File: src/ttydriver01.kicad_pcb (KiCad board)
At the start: 2 copper layers, 119.4 x 74.9 mm, 34 parts, among them P1 CONN_01X04, P2 CONN_01X02, P3 CONN_01X02, P4 CONN_01X10, Q1 IRLB8721PBF, T1 Coilcraft-DA2032, U1 NE555, U2 TPS2030P, U3 CP2102-breakout, U4 G3VM401E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

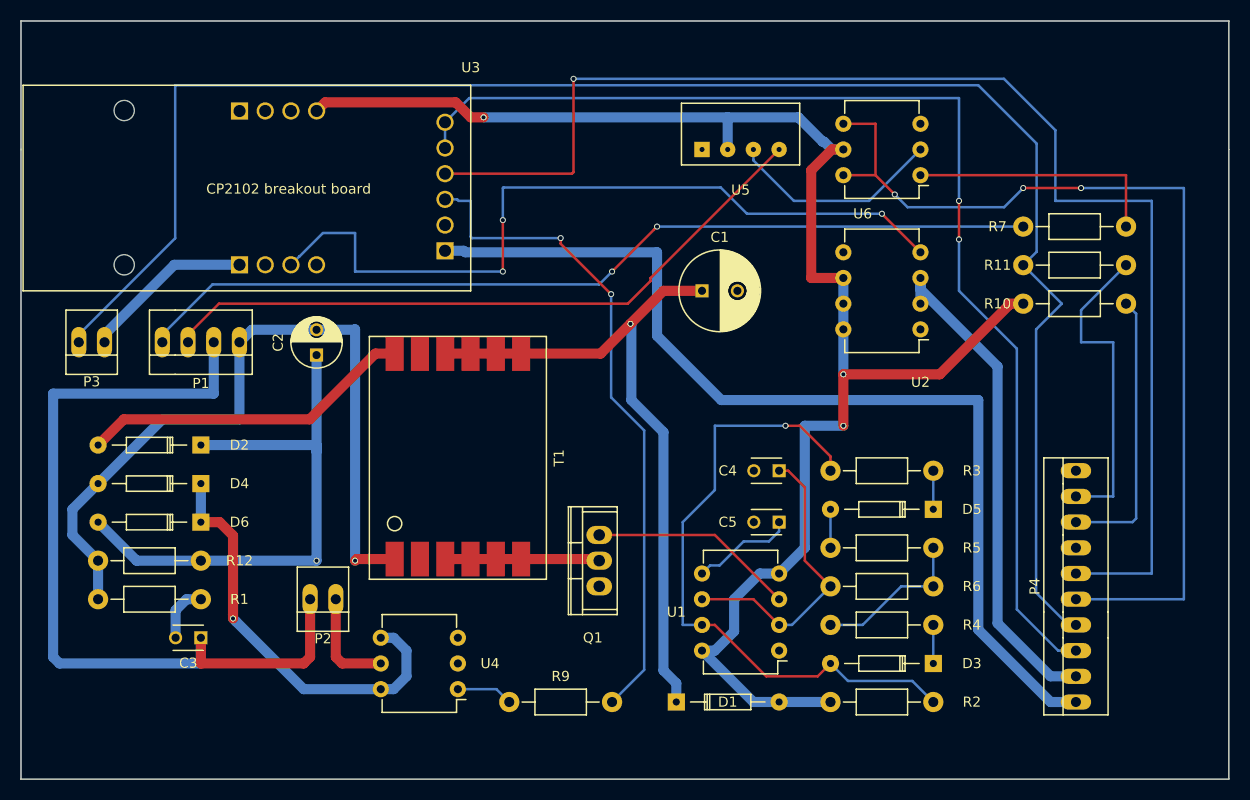
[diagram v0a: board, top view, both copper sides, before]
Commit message: Passes DRC. Valid board.  Still needs more cleanup.
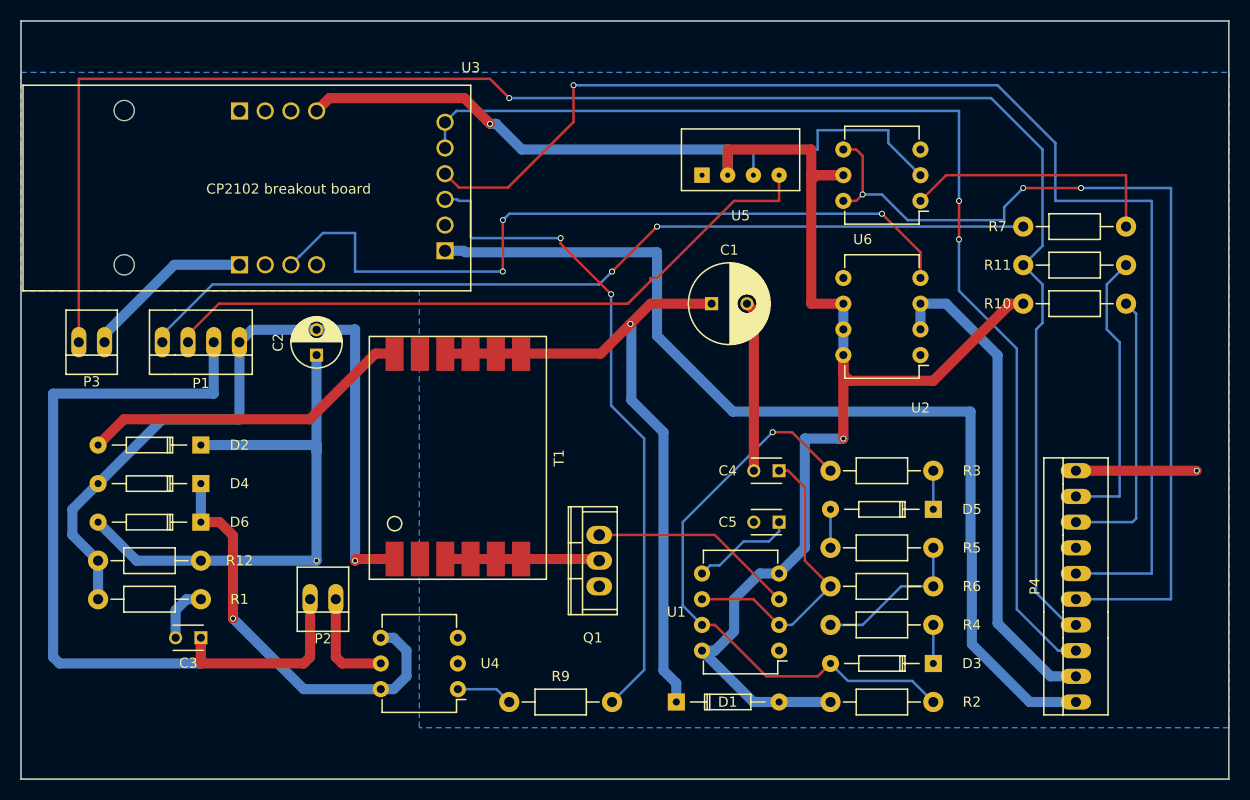
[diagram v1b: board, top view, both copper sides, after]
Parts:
- moved U6 2.54 mm to (144.8, 95.2)
- moved U2 2.54 mm to (144.8, 110.5)
- moved U5 2.54 mm to (127.0, 92.7)
- moved C1 1.58 mm to (124.1, 105.4)
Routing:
- net GND: track 17.0 -> 45.7 mm, vias 0 -> 1
- net Net-(D3-Pad2): track 64.1 -> 57.9 mm
- net Net-(P3-Pad2): track 169.7 -> 175.8 mm, vias 0 -> 1
- net VCC: track 157.6 -> 163.2 mm, vias 3 -> 2
- net /RxD: track 95.3 -> 91.8 mm
- net Net-(P4-Pad6): track 132.6 -> 129.1 mm
- net Net-(P4-Pad9): track 31.6 -> 28.5 mm
- net Net-(U5-Pad3): track 21.3 -> 23.5 mm
- net Net-(P4-Pad3): track 114.8 -> 113.0 mm
- net /ENABLE: track 78.3 -> 76.8 mm
- net Net-(R7-Pad2): track 25.4 -> 26.5 mm
- net Net-(P4-Pad2): track 49.7 -> 48.7 mm
- added copper zone on B.Cu, net GND

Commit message: Passes DRC. Valid board.  Still needs more cleanup.
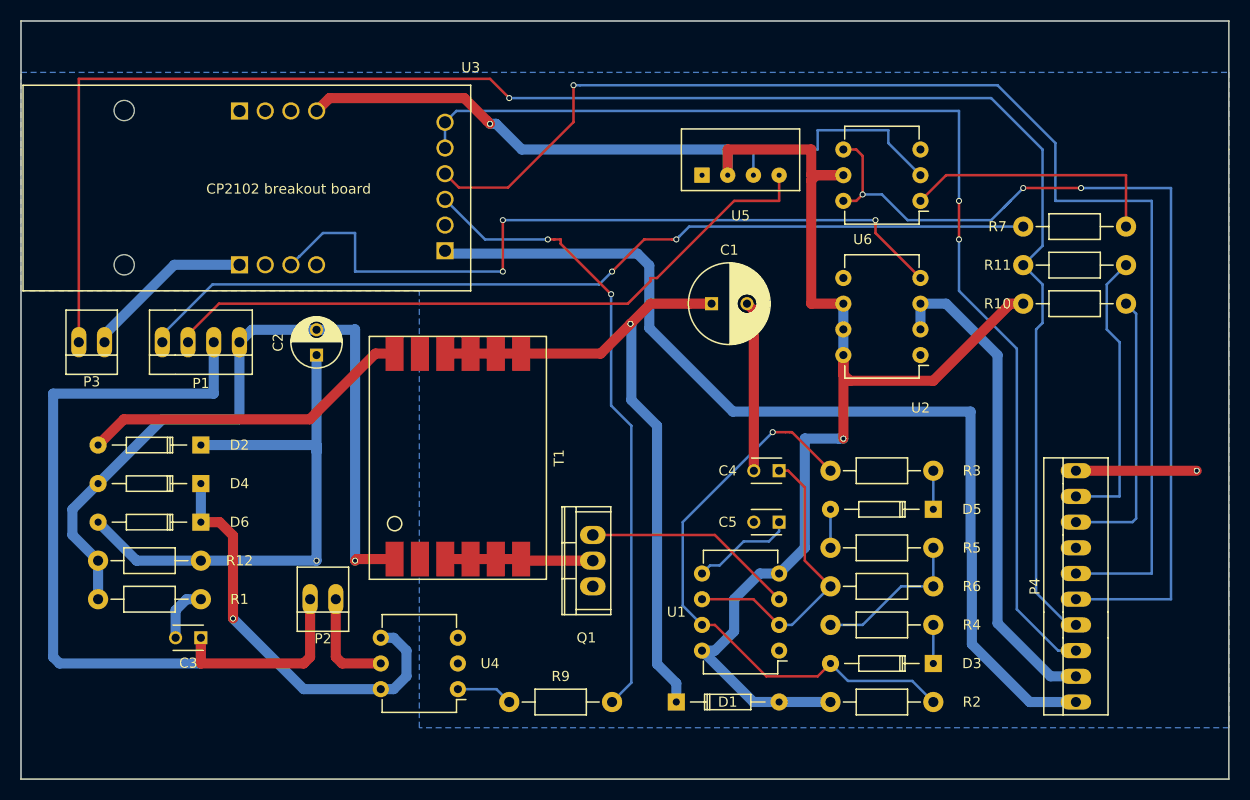
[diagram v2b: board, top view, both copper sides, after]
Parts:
- moved Q1 0.64 mm to (112.4, 130.8)
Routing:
- net /TxD: track 65.7 -> 62.7 mm
- net /ENABLE: track 76.8 -> 75.5 mm
- net Net-(P4-Pad1): track 99.1 -> 97.8 mm
- net /OSC: track 20.4 -> 21.0 mm

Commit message: Cleaned up copper fill. Almost ready for fab.
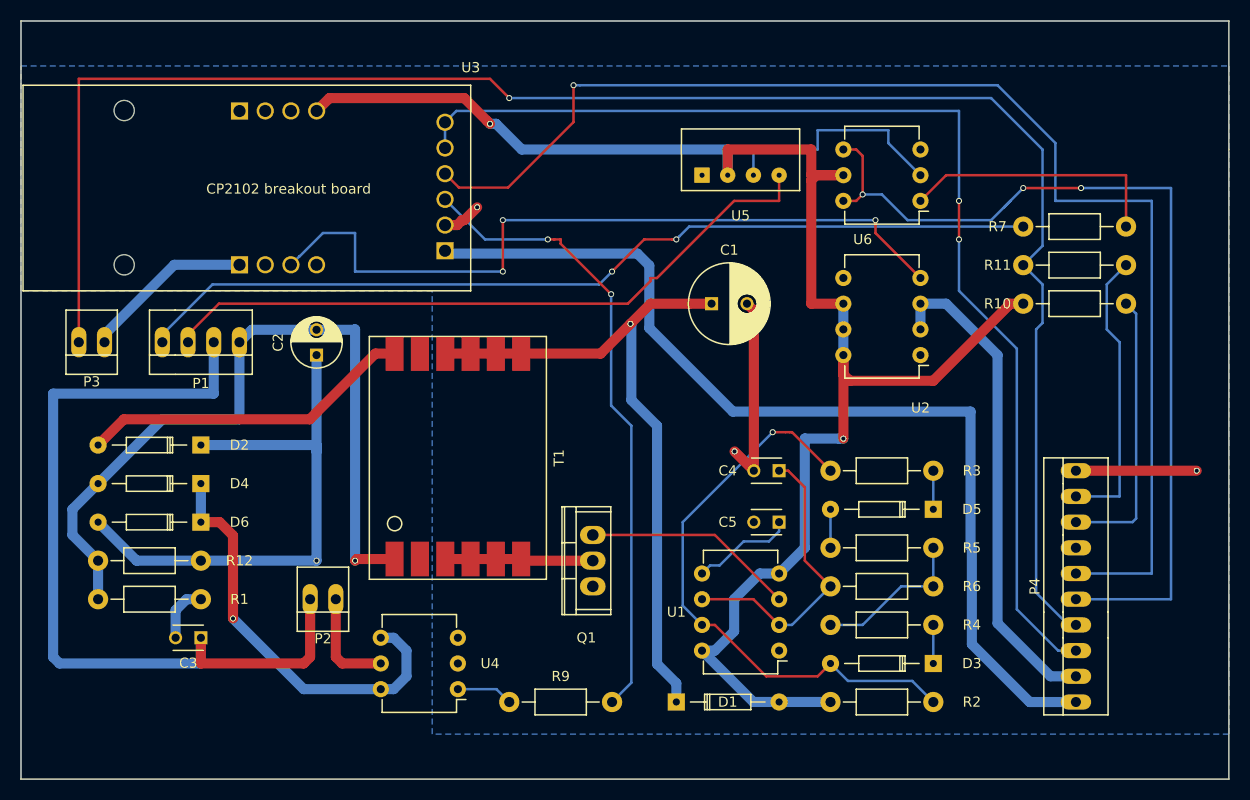
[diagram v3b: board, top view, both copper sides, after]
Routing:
- net GND: track 45.7 -> 52.3 mm, vias 1 -> 3
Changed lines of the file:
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@@
     (thickness 1.6)
     (drawings 8)
-    (tracks 310)
+    (tracks 317)
     (zones 0)
     (modules 34)
@@
     (last_trace_width 0.25)
     (trace_clearance 0.2)
-    (zone_clearance 0.508)
+    (zone_clearance 0.6)
     (zone_45_only yes)
     (trace_min 0.2)
@@
   (segment (start 123.19 134.62) (end 128.27 134.62) (width 0.25) (layer F.Cu) (net 1) (status 10))
   (segment (start 128.27 134.62) (end 130.81 137.16) (width 0.25) (layer F.Cu) (net 1) (status 20))
+  (via (at 126.405 120.015) (size 0.6) (drill 0.4) (layers F.Cu B.Cu) (net 2))
+  (segment (start 128.31 121.92) (end 126.405 120.015) (width 1) (layer F.Cu) (net 2))
+  (segment (start 99.695 97.155) (end 100.965 95.885) (width 1) (layer F.Cu) (net 2))
+  (via (at 100.965 95.885) (size 0.6) (drill 0.4) (layers F.Cu B.Cu) (net 2))
+  (segment (start 99.477081 97.155) (end 99.695 97.155) (width 1) (layer F.Cu) (net 2))
+  (segment (start 97.79 97.64) (end 98.992081 97.64) (width 1) (layer F.Cu) (net 2))
+  (segment (start 98.992081 97.64) (end 99.477081 97.155) (width 1) (layer F.Cu) (net 2))
   (segment (start 128.31 121.92) (end 128.31 106.085) (width 1) (layer F.Cu) (net 2))
   (segment (start 128.31 106.085) (end 127.635 105.41) (width 1) (layer F.Cu) (net 2))
@@
     (connect_pads (clearance 0.508))
     (min_thickness 0.254)
-    (keepout (tracks not_allowed) (vias not_allowed) (copperpour not_allowed))
-    (fill (arc_segments 16) (thermal_gap 1) (thermal_bridge_width 1))
-    (polygon
-      (pts
-        (xy 175.26 82.55) (xy 55.88 82.55) (xy 55.88 77.47) (xy 175.26 77.47)
-      )
-    )
-  )
-  (zone (net 0) (net_name "") (layer F.Cu) (hatch edge 0.508)
-    (connect_pads (clearance 0.508))
-    (min_thickness 0.254)
     (keepout (tracks allowed) (vias allowed) (copperpour not_allowed))
     (fill (arc_segments 16) (thermal_gap 1) (thermal_bridge_width 1))
@@
     )
   )
-  (zone (net 2) (net_name GND) (layer B.Cu) (hatch edge 0.508)
+  (zone (net 0) (net_name "") (layer F.Cu) (hatch edge 0.508)
     (connect_pads (clearance 0.508))
     (min_thickness 0.254)
-    (fill yes (arc_segments 16) (thermal_gap 1) (thermal_bridge_width 1))
+    (keepout (tracks not_allowed) (vias not_allowed) (copperpour not_allowed))
+    (fill (arc_segments 16) (thermal_gap 1) (thermal_bridge_width 1))
     (polygon
       (pts
-        (xy 175.26 82.55) (xy 175.26 147.32) (xy 95.25 147.32) (xy 95.25 104.14) (xy 55.88 104.14)
-        (xy 55.88 82.55)
+        (xy 175.26 82.55) (xy 55.88 82.55) (xy 55.88 77.47) (xy 175.26 77.47)
       )
     )
+  )
+  (zone (net 2) (net_name GND) (layer B.Cu) (hatch edge 0.508)
+    (connect_pads (clearance 0.6))
+    (min_thickness 0.6)
+    (fill yes (arc_segments 16) (thermal_gap 0.7) (thermal_bridge_width 1))
+    (polygon
+      (pts
+        (xy 175.26 81.915) (xy 175.26 147.955) (xy 96.52 147.955) (xy 96.52 104.14) (xy 55.88 104.14)
+        (xy 55.88 81.915)
+      )
+    )

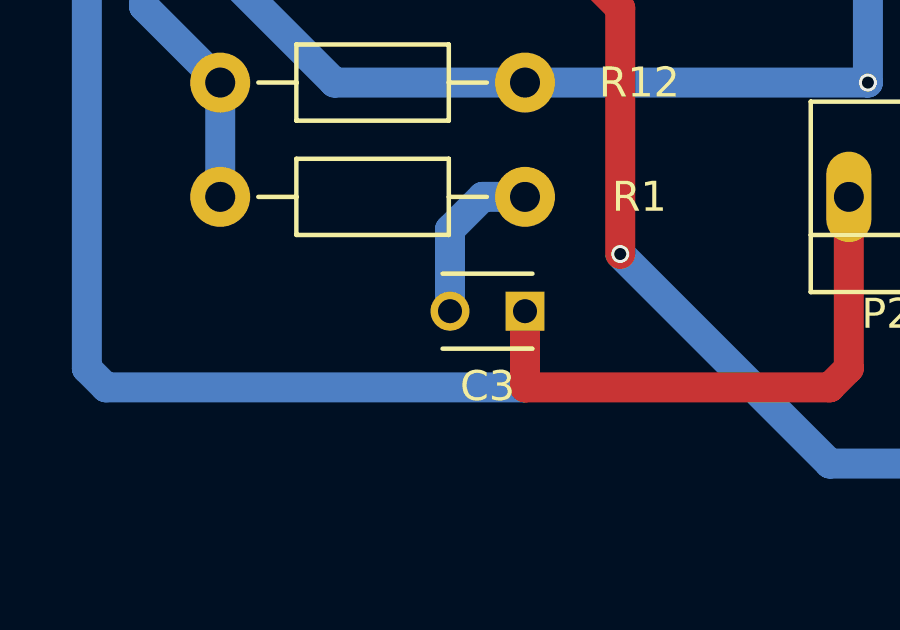
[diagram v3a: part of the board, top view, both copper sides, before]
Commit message: All caps added. Just resistors left to add to BOM
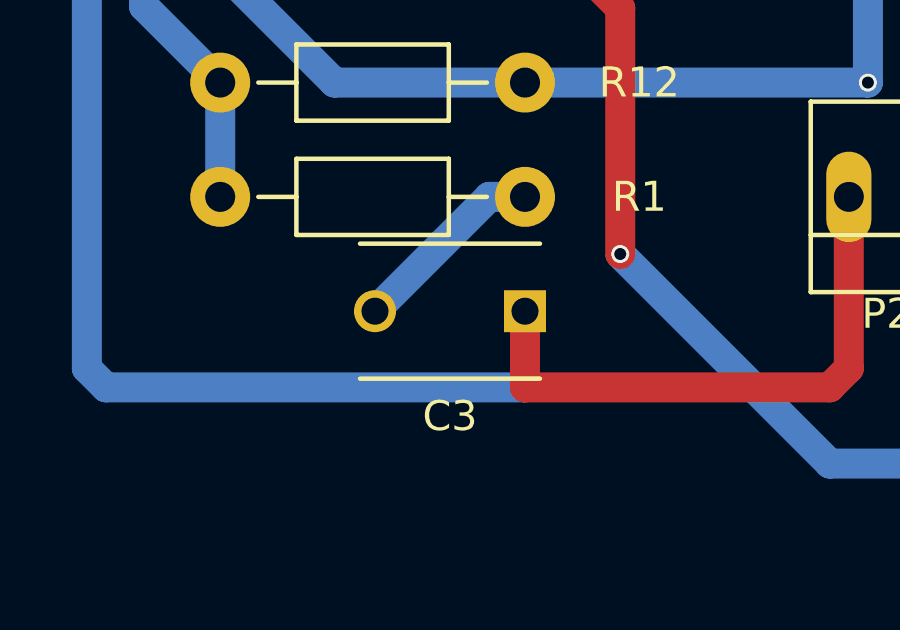
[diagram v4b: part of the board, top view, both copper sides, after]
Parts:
- C3: footprint Capacitors_ThroughHole:C_Disc_D3_P2.5 -> Capacitors_ThroughHole:C_Disc_D6_P5
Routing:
- net Net-(C3-Pad2): track 5.67 -> 6.58 mm
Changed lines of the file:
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@@
     (links 78)
     (no_connects 0)
-    (area 55.404999 77.394999 193.291156 161.450001)
+    (area 55.804999 77.394999 175.335001 152.475001)
     (thickness 1.6)
     (drawings 8)
-    (tracks 317)
+    (tracks 316)
     (zones 0)
     (modules 34)
@@
   )
   (module Capacitors_ThroughHole:C_Disc_D3_P2.5 (layer F.Cu)
-    (at 73.66 138.43 180)
-    (descr "Capacitor 3mm Disc, Pitch 2.5mm")
-    (tags Capacitor)
-    (fp_text reference C3 (at 1.25 -2.5 180) (layer F.SilkS)
-      (effects (font (size 1 1) (thickness 0.15)))
-    )
-    (fp_text value 1000pf (at 1.25 2.5 180) (layer F.Fab)
-      (effects (font (size 1 1) (thickness 0.15)))
-    )
-    (fp_line (start -0.9 -1.5) (end 3.4 -1.5) (layer F.CrtYd) (width 0.05))
-    (fp_line (start 3.4 -1.5) (end 3.4 1.5) (layer F.CrtYd) (width 0.05))
-    (fp_line (start 3.4 1.5) (end -0.9 1.5) (layer F.CrtYd) (width 0.05))
-    (fp_line (start -0.9 1.5) (end -0.9 -1.5) (layer F.CrtYd) (width 0.05))
-    (fp_line (start -0.25 -1.25) (end 2.75 -1.25) (layer F.SilkS) (width 0.15))
-    (fp_line (start 2.75 1.25) (end -0.25 1.25) (layer F.SilkS) (width 0.15))
-    (pad 1 thru_hole rect (at 0 0 180) (size 1.3 1.3) (drill 0.8) (layers *.Cu *.Mask F.SilkS)
-      (net 41 /HVPOS))
-    (pad 2 thru_hole circle (at 2.5 0 180) (size 1.3 1.3) (drill 0.8001) (layers *.Cu *.Mask F.SilkS)
-      (net 23 "Net-(C3-Pad2)"))
-    (model Capacitors_ThroughHole.3dshapes/C_Disc_D3_P2.5.wrl
-      (at (xyz 0.0492126 0 0))
-      (scale (xyz 1 1 1))
-      (rotate (xyz 0 0 0))
-    )
-  )
-  (module Capacitors_ThroughHole:C_Disc_D3_P2.5 (layer F.Cu)
     (at 130.81 121.92 180)
     (descr "Capacitor 3mm Disc, Pitch 2.5mm")
@@
     (pad 1 thru_hole oval (at -2.54 0 90) (size 1.8 2.54) (drill 1.143) (layers *.Cu *.Mask F.SilkS)
       (net 2 GND))
+  )
+  (module Capacitors_ThroughHole:C_Disc_D6_P5 (layer F.Cu)
+    (at 73.66 138.43 180)
+    (descr "Capacitor 6mm Disc, Pitch 5mm")
+    (tags Capacitor)
+    (fp_text reference C3 (at 2.5 -3.5 180) (layer F.SilkS)
+      (effects (font (size 1 1) (thickness 0.15)))
+    )
+    (fp_text value 1000pf (at 2.5 3.5 180) (layer F.Fab)
+      (effects (font (size 1 1) (thickness 0.15)))
+    )
+    (fp_line (start -0.95 -2.5) (end 5.95 -2.5) (layer F.CrtYd) (width 0.05))
+    (fp_line (start 5.95 -2.5) (end 5.95 2.5) (layer F.CrtYd) (width 0.05))
+    (fp_line (start 5.95 2.5) (end -0.95 2.5) (layer F.CrtYd) (width 0.05))
+    (fp_line (start -0.95 2.5) (end -0.95 -2.5) (layer F.CrtYd) (width 0.05))
+    (fp_line (start -0.5 -2.25) (end 5.5 -2.25) (layer F.SilkS) (width 0.15))
+    (fp_line (start 5.5 2.25) (end -0.5 2.25) (layer F.SilkS) (width 0.15))
+    (pad 1 thru_hole rect (at 0 0 180) (size 1.4 1.4) (drill 0.9) (layers *.Cu *.Mask F.SilkS)
+      (net 41 /HVPOS))
+    (pad 2 thru_hole circle (at 5 0 180) (size 1.4 1.4) (drill 0.9) (layers *.Cu *.Mask F.SilkS)
+      (net 23 "Net-(C3-Pad2)"))
+    (model Capacitors_ThroughHole.3dshapes/C_Disc_D6_P5.wrl
+      (at (xyz 0.0984252 0 0))
+      (scale (xyz 1 1 1))
+      (rotate (xyz 0 0 0))
+    )
   )
   (gr_line (start 175.26 90.17) (end 175.26 77.47) (angle 90) (layer Edge.Cuts) (width 0.15))
@@
   (segment (start 73.66 130.81) (end 85.09 130.81) (width 1) (layer B.Cu) (net 22) (status 10))
   (segment (start 85.09 130.81) (end 85.09 120.015) (width 1) (layer B.Cu) (net 22))
-  (segment (start 73.66 134.62) (end 72.246508 134.62) (width 1) (layer B.Cu) (net 23) (status 10))
-  (segment (start 72.246508 134.62) (end 71.16 135.706508) (width 1) (layer B.Cu) (net 23))
-  (segment (start 71.16 135.706508) (end 71.16 138.43) (width 1) (layer B.Cu) (net 23) (status 20))
+  (segment (start 73.66 134.62) (end 72.47 134.62) (width 1) (layer B.Cu) (net 23))
+  (segment (start 72.47 134.62) (end 68.66 138.43) (width 1) (layer B.Cu) (net 23))
   (segment (start 92.81 110.34) (end 90.915 110.34) (width 1) (layer F.Cu) (net 24) (status 10))
   (segment (start 90.915 110.34) (end 84.415 116.84) (width 1) (layer F.Cu) (net 24))
